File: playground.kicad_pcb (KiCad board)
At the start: 2 copper layers, 80 x 80 mm, 74 parts, among them IC1 TXU0101DBVR, IC11 LM3940IMP-3.3_NOPB, IC2 TXU0101DBVR, IC3 TXU0101DBVR, IC4 TXU0101DBVR, IC5 TXU0101DBVR, IC6 TXU0101DBVR, IC7 TXU0101DBVR, IC8 TXU0101DBVR, IC9 L293DD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

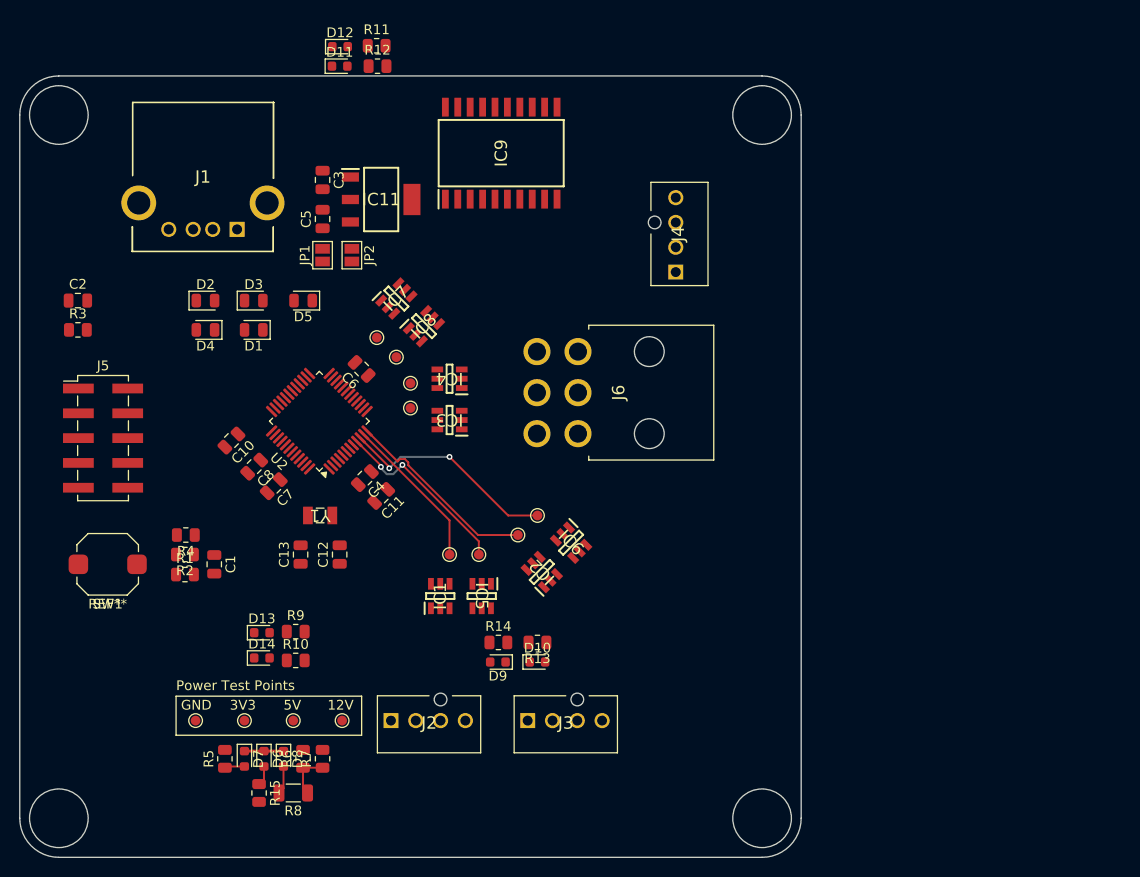
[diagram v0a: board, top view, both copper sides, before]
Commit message: Reduced board size
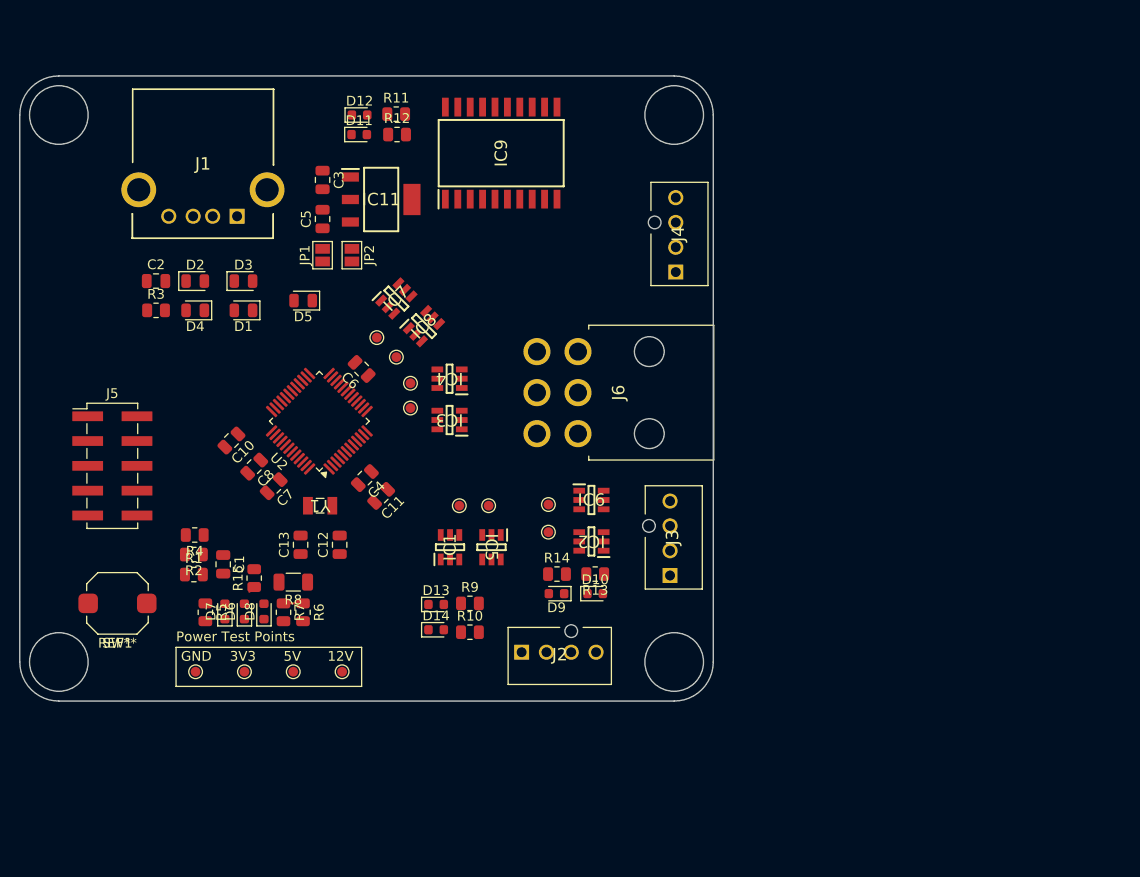
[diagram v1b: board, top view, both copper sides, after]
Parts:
- moved R15 22.0 mm to (74.0, 101.4), turned to 90 degrees
- moved R8 21.6 mm to (78.0, 101.8)
- moved J3 20.8 mm to (116.6, 101.1), turned to -90 degrees
- moved D13 18.1 mm to (92.6, 104.1)
- moved D14 18.1 mm to (92.6, 106.7)
- moved R10 18.1 mm to (96.1, 107.0)
- moved R9 18.1 mm to (96.1, 104.0)
- moved R7 15.5 mm to (77.0, 104.9), turned to -90 degrees
- moved D6 15.2 mm to (73.0, 104.8), turned to 90 degrees
- moved D7 15.2 mm to (71.0, 104.8), turned to 90 degrees
- moved D8 15.2 mm to (75.0, 104.8), turned to 90 degrees
- moved R5 15.1 mm to (69.0, 104.9), turned to -90 degrees
- moved J2 15.1 mm to (101.4, 109.0)
- moved R6 15.0 mm to (79.0, 104.9), turned to -90 degrees
- moved D9 9.22 mm to (105.0, 103.0)
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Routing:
- net /FanCtrl_3v3: track 22.5 -> 0.00 mm, vias 2 -> 0
- net /FanSense_3v3: track 20.2 -> 0.00 mm
- net /PumpCtrl_3v3: track 19.0 -> 0.00 mm, vias 2 -> 0
- net /PumpSense_3v3: track 15.9 -> 0.00 mm
- net GND: track 4.00 -> 0.00 mm
- net /LEDs/12v_PWR_IND_LED: track 2.90 -> 0.00 mm
- net /LEDs/12v_PWD_LED_VOL_DIV: track 4.78 -> 2.00 mm
- net /LEDs/3v3_PWR_IND_LED: track 2.05 -> 0.00 mm
- net /LEDs/5v_USB_PWR_IND_LED: track 2.01 -> 0.71 mm
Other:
- board size 80 x 80 mm -> 71 x 64 mm

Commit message: Initial Routing
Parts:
- removed D13: GENERAL_BOARD_1_IND, LED_SMD:LED_0603_1608Metric
- removed D14: GENERAL_BOARD_2_IND, LED_SMD:LED_0603_1608Metric
- removed R10, R9: 51R, Resistor_SMD:R_0805_2012Metric
- moved D11 27.6 mm to (108.0, 70.8), turned to 90 degrees
- moved D12 27.1 mm to (106.0, 70.8), turned to 90 degrees
- moved R12 26.1 mm to (110.0, 71.0), turned to -90 degrees
- moved R11 23.0 mm to (104.0, 71.0), turned to -90 degrees
- moved TP5 2.24 mm to (96.0, 95.0)
- moved JP1 1.70 mm to (81.0, 66.7)
- moved JP2 1.70 mm to (84.0, 66.7)
- moved C3 1.70 mm to (81.0, 59.0)
- moved IC11 1.70 mm to (87.0, 61.0)
- moved C5 1.70 mm to (81.0, 63.0)
- moved TP9 1.00 mm to (94.0, 94.0)
- moved TP7 0.56 mm to (86.0, 76.8)
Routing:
- net GND: track 0.00 -> 145.8 mm, vias 0 -> 34
- net +12V: track 0.00 -> 119.1 mm
- net +5V: track 0.00 -> 110.1 mm, vias 0 -> 2
- net +3V3: track 0.00 -> 98.5 mm, vias 0 -> 9
- net /RESET: track 0.00 -> 40.0 mm, vias 0 -> 4
- net /ValveSense1_5v: track 0.00 -> 35.2 mm, vias 0 -> 4
- net /SWCLK: track 0.00 -> 32.0 mm, vias 0 -> 2
- net /ValveSense2_5v: track 0.00 -> 28.5 mm, vias 0 -> 2
- net /FanCtrl_3v3: track 0.00 -> 28.1 mm
- net /FanSense_3v3: track 0.00 -> 26.0 mm
- net /usb_shield_gnd: track 0.00 -> 25.8 mm
- net /USB_D+: track 0.00 -> 25.1 mm
- net /USB_D-: track 0.00 -> 24.1 mm
- net /PumpCtrl_5v: track 0.00 -> 23.4 mm
- net /SWDIO: track 0.00 -> 23.3 mm
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- added copper zone on F.Cu, net +3V3
- added copper zone on F.Cu, net +5V
- added copper zone on B.Cu, net GND

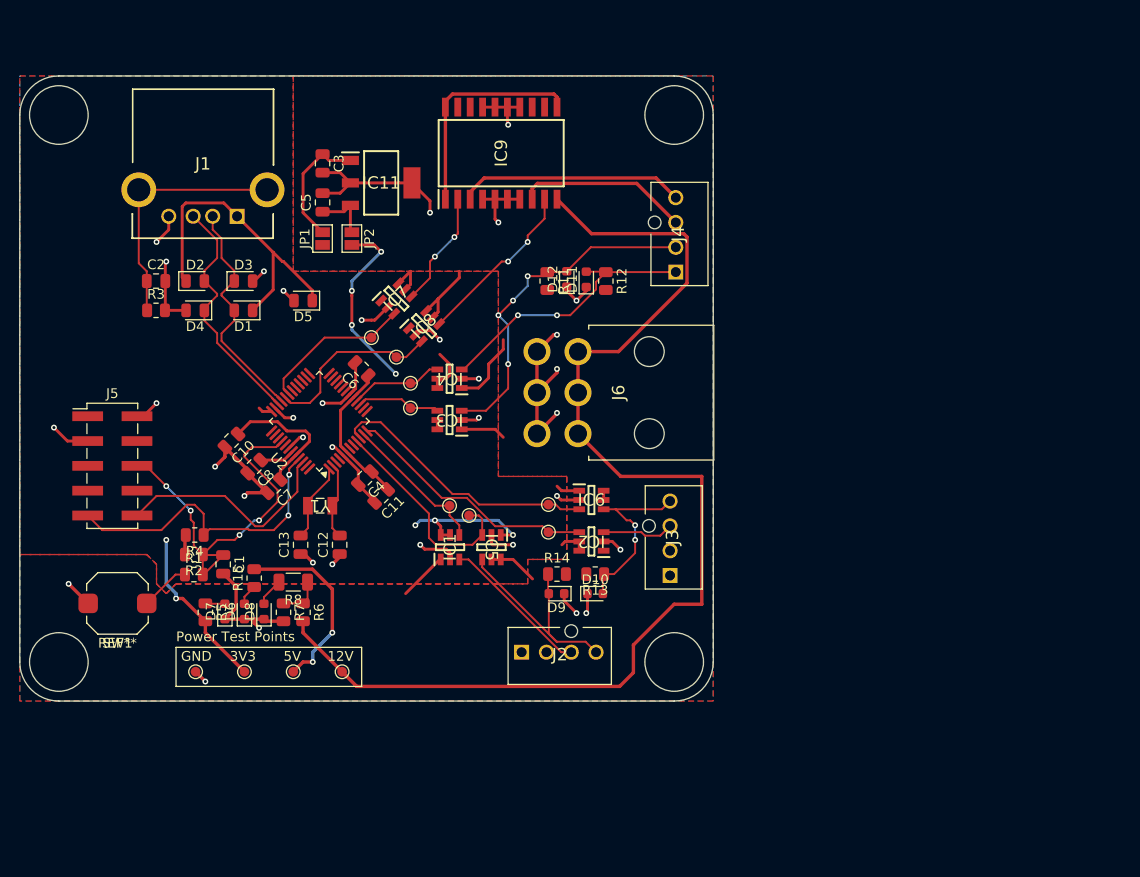
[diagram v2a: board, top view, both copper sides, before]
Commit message: Completed intial 2-layer routing.
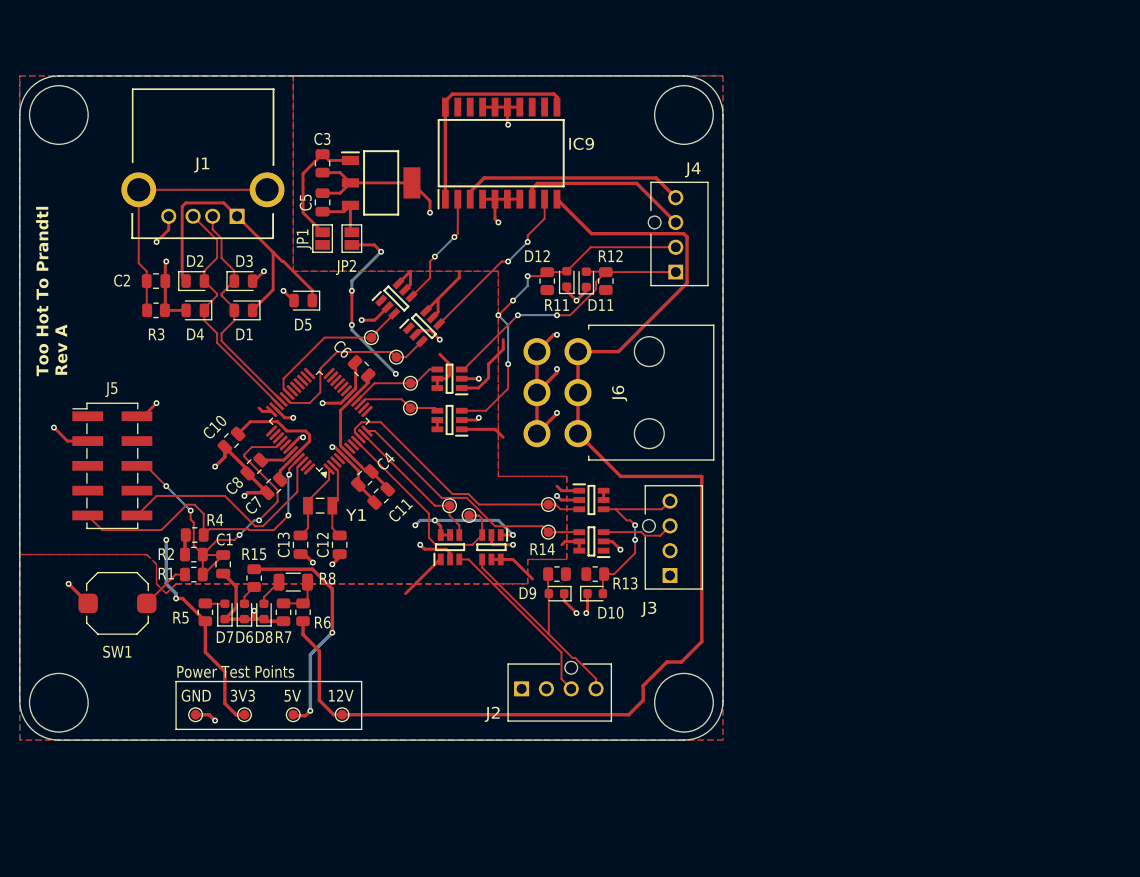
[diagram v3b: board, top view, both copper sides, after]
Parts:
- moved TP1 4.40 mm to (83.0, 115.4)
- moved TP2 4.40 mm to (78.0, 115.4)
- moved TP3 4.40 mm to (73.0, 115.4)
- moved TP4 4.40 mm to (68.0, 115.4)
- moved J2 3.75 mm to (101.4, 112.8)
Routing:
- net +12V: track 119.1 -> 126.0 mm
- net +3V3: track 98.5 -> 103.4 mm
- net +5V: track 110.1 -> 114.8 mm
- net /PumpSense_5v: track 15.4 -> 18.5 mm
- net /PumpCtrl_5v: track 23.4 -> 24.4 mm
- net GND: track 145.8 -> 146.4 mm
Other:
- board size 71 x 64 mm -> 72 x 68 mm
- board text added: "Too Hot To Prandtl Rev A"

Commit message: Initial Layout
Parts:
- added H1: MountingHole_Pad, MountingHole:MountingHole_2.2mm_M2_Pad, F.Cu at (158.0, 63.0)
- added H2: MountingHole_Pad, MountingHole:MountingHole_2.2mm_M2_Pad, F.Cu at (158.5, 106.0)
- added H3: MountingHole_Pad, MountingHole:MountingHole_2.2mm_M2_Pad, F.Cu at (85.0, 63.0)
- added H4: MountingHole_Pad, MountingHole:MountingHole_2.2mm_M2_Pad, F.Cu at (85.5, 105.5)
- J5: footprint Connector_PinHeader_2.54mm:PinHeader_2x05_P2.54mm_Vertical_SMD -> Connector_PinHeader_2.54mm:PinHeader_2x05_P2.54mm_Vertical
- moved J5 91.5 mm to (150.1, 102.5), turned to -90 degrees
- moved TP4 88.7 mm to (145.9, 73.0)
- moved D8 87.2 mm to (153.8, 67.5), turned to 180 degrees
- moved TP3 86.9 mm to (148.9, 73.1)
- moved R7 86.1 mm to (153.5, 65.5), turned to 0 degrees
- moved R6 85.8 mm to (157.5, 70.2)
- moved D6 85.4 mm to (149.8, 67.5), turned to 180 degrees
- moved TP2 85.1 mm to (151.9, 73.1)
- moved R5 84.6 mm to (145.8, 69.5), turned to 0 degrees
- moved D7 83.6 mm to (145.8, 67.5), turned to 180 degrees
- moved TP1 83.4 mm to (154.9, 73.1)
- moved R8 82.5 mm to (153.9, 69.5)
- moved R15 82.3 mm to (149.8, 69.5), turned to 0 degrees
- moved R4 68.4 mm to (136.1, 102.0), turned to -90 degrees
- moved J2 60.4 mm to (155.8, 86.5), turned to -90 degrees
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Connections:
- net Net-(R1-Pad1) renamed /RST_SW_R
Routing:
- net GND: track 146.4 -> 0.00 mm, vias 34 -> 0
- net +12V: track 126.0 -> 0.00 mm
- net +5V: track 114.8 -> 0.00 mm, vias 2 -> 0
- net +3V3: track 103.4 -> 0.00 mm, vias 9 -> 0
- net /RESET: track 40.0 -> 0.00 mm, vias 4 -> 0
- net /ValveSense1_5v: track 35.2 -> 0.00 mm, vias 4 -> 0
- net /SWCLK: track 32.0 -> 0.00 mm, vias 2 -> 0
- net /ValveSense2_5v: track 28.5 -> 0.00 mm, vias 2 -> 0
- net /FanCtrl_3v3: track 28.1 -> 0.00 mm
- net /FanSense_3v3: track 26.0 -> 0.00 mm
- net /usb_shield_gnd: track 25.8 -> 0.00 mm
- net /USB_D+: track 25.1 -> 0.00 mm
- net /PumpCtrl_5v: track 24.4 -> 0.00 mm
- net /USB_D-: track 24.1 -> 0.00 mm
- net /SWDIO: track 23.3 -> 0.00 mm
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- removed copper zone on F.Cu, net +3V3
- removed copper zone on F.Cu, net +5V
- removed copper zone on B.Cu, net GND
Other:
- board size 72 x 68 mm -> 80.5 x 50.5 mm
- copper layers 2 -> 4
- board text added: "FAN"
- board text added: "PUMP"
- board text added: "SWD Header"
- board text added: "Too Hot Too Prandtl Rev A 3/24"
- board text added: "VALVE"
- board text removed: "Power Test Points"
- board text removed: "Too Hot To Prandtl Rev A"
